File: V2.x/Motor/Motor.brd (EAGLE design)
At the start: 43.2 x 34.3 mm, 48 parts, among them IC1 Atmega 328-P, IC2 MCP2515, IC3 LM340MP-05, Q1 8MHz, Q2 16MHz

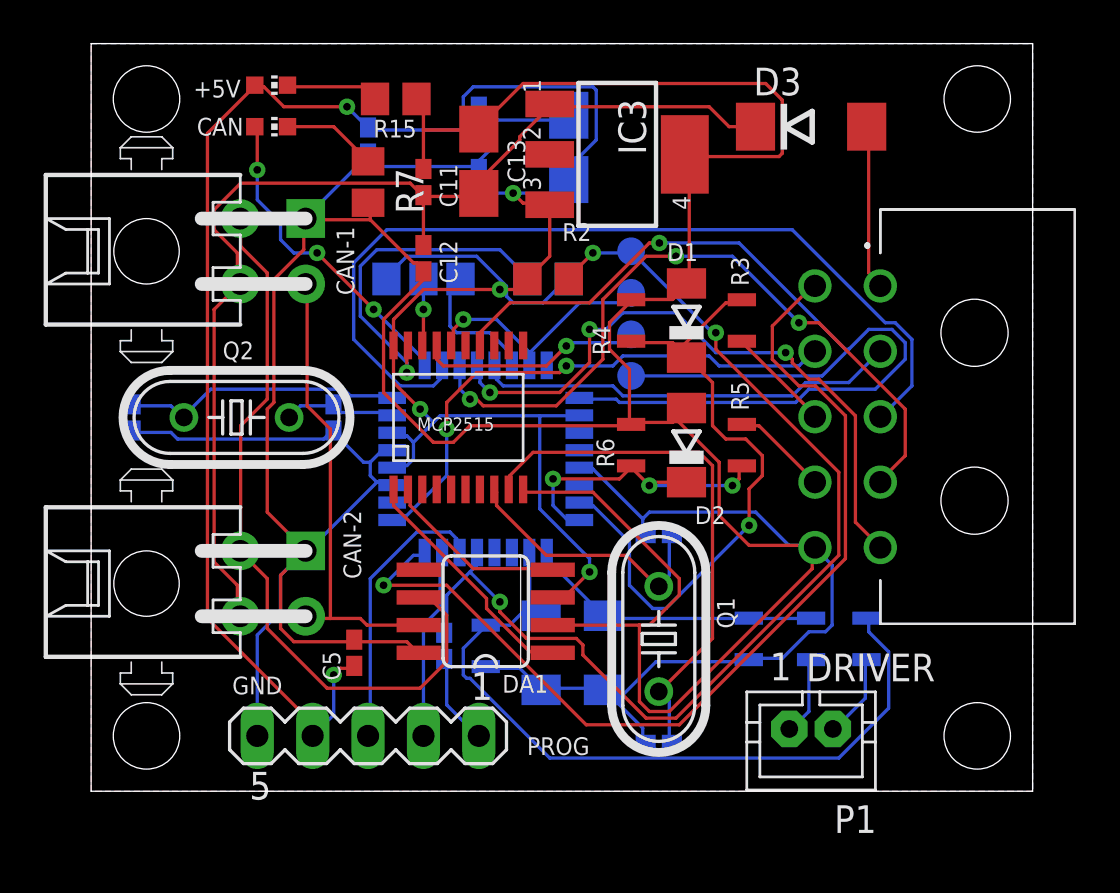
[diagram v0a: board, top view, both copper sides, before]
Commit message: added Loco-CAN icon to motor, servo and switch boards
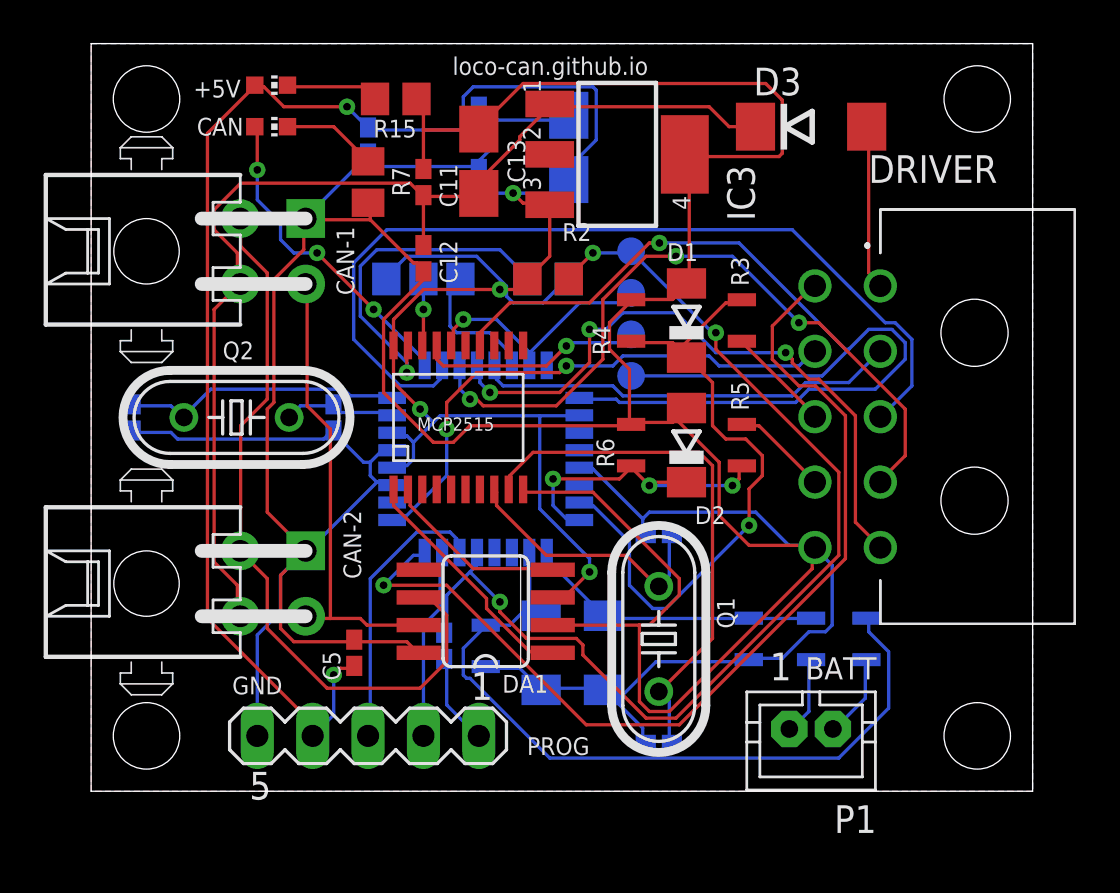
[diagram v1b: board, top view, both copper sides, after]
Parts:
- renumbered RST to RS
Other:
- board text added: "BATT"
- board text added: "ISP"
- board text added: "Motor"
- board text added: "V2.2"
- board text added: "loco-can.github.io"
- board text removed: "10"
- board text removed: "11"
- board text removed: "12"
- board text removed: "13"
- board text removed: "LOCO-Motor"
- board text removed: "UNO-ISP"
- board text removed: "V2.2-s"
